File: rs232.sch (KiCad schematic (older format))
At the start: 7 parts, among them Q1 BC847, U4 MAX3188EEUT+T

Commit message: Use smaller jumper
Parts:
- removed JP2: SolderJumper_2_Bridged, Jumpers:SMT-JUMPER_2_NO_SILK, symbol Jumper:SolderJumper_2_Bridged
- JP1: footprint Connector_PinHeader_2.54mm:PinHeader_2x01_P2.54mm_Vertical -> Connector_PinHeader_1.00mm:PinHeader_1x02_P1.00mm_Vertical
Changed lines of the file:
@@
 $Descr A4 11693 8268
 encoding utf-8
-Sheet 5 5
+Sheet 4 5
 Title ""
 Date ""
@@
 F 0 "JP1" H 5600 3953 50  0000 C CNN
 F 1 "Jumper_2_Bridged" H 5600 3954 50  0001 C CNN
-F 2 "Connector_PinHeader_2.54mm:PinHeader_2x01_P2.54mm_Vertical" H 5600 3850 50  0001 C CNN
+F 2 "Connector_PinHeader_1.00mm:PinHeader_1x02_P1.00mm_Vertical" H 5600 3850 50  0001 C CNN
 F 3 "~" H 5600 3850 50  0001 C CNN
 	1    5600 3850
@@
 Wire Wire Line
 	5350 2900 6300 2900
-Wire Wire Line
-	5250 3850 5400 3850
 $Comp
 L Device:R R?
@@
 Wire Wire Line
 	5400 4750 5400 4900
-$Comp
-L Jumper:SolderJumper_2_Bridged JP?
-U 1 1 5ED0E3F3
-P 5600 4000
-AR Path="/5ED0E3F3" Ref="JP?"  Part="1"
-AR Path="/5ED01473/5ED0E3F3" Ref="JP2"  Part="1"
-F 0 "JP2" H 5600 4113 50  0000 C CNN
-F 1 "SolderJumper_2_Bridged" H 5600 4114 50  0001 C CNN
-F 2 "Jumpers:SMT-JUMPER_2_NO_SILK" H 5600 4000 50  0001 C CNN
-F 3 "~" H 5600 4000 50  0001 C CNN
-	1    5600 4000
-	1    0    0    -1
-$EndComp
 Wire Notes Line
 	6500 3700 6500 4100
 Wire Notes Line
 	5200 3700 5200 4100
-Wire Wire Line
-	5450 4000 5250 4000
-Wire Wire Line
-	5250 4000 5250 3850
-Wire Wire Line
-	5750 4000 5950 4000
-Wire Wire Line
-	5950 3850 5950 4000
-Wire Wire Line
-	5950 4000 5950 4200
-Connection ~ 5950 4000
 $Comp
 L Transistor_BJT:BC847 Q?
@@
 Text HLabel 5150 3850 0    50   BiDi ~ 0
 UPDI
-Wire Wire Line
-	5250 3850 5150 3850
-Connection ~ 5250 3850
 Text HLabel 5150 4900 0    50   Output ~ 0
 RX
@@
 	5400 4900 5150 4900
 Connection ~ 5400 4900
+Wire Wire Line
+	5950 3850 5950 4200
+Wire Wire Line
+	5150 3850 5400 3850
 $EndSCHEMATC

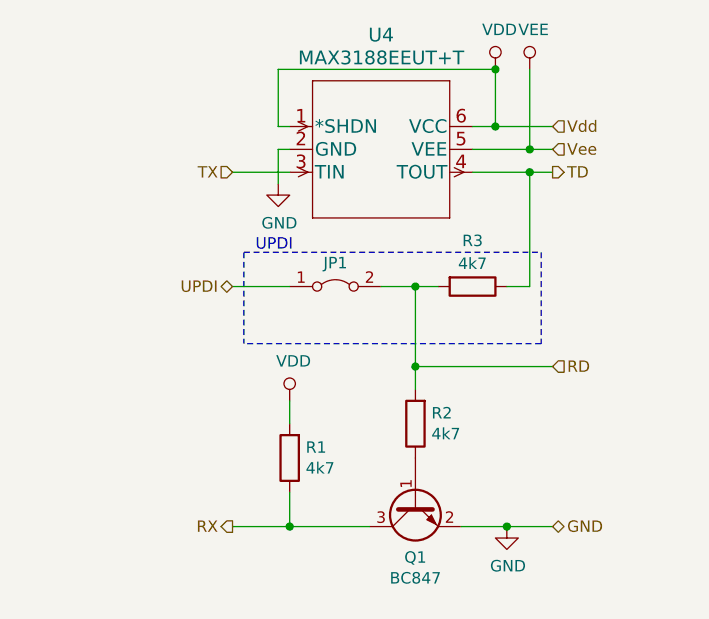
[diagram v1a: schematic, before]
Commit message: Use MAX3180 for incoming RS-232
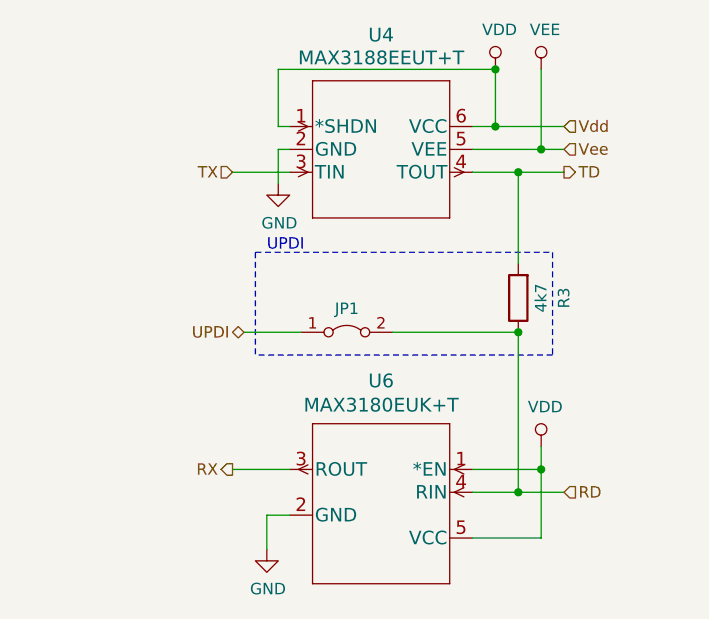
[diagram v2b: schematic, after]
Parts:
- removed Q1: BC847, Package_TO_SOT_SMD:SOT-23, symbol Transistor_BJT:BC847
- removed R1, R2: 4k7, Resistors_SMD:R_0603_HandSoldering, symbol Device:R
- added U6: MAX3180EUK+T, Package_TO_SOT_SMD:SOT-23-5_HandSoldering, symbol MAX3180:MAX3180EUK+T
- U4: footprint MAX3188:MAX3188EEUT&plus_T -> Package_TO_SOT_SMD:SOT-23-5_HandSoldering
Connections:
- net GND: now also U6.2 (GND)
- net RD: now also R3.1, U6.4 (RIN); no longer R3.2
- net RX: now also U6.3 (ROUT)
- net TD: now also R3.2; no longer R3.1
- net VDD: now also U6.1 (*EN), U6.5 (VCC)
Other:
- moved on the sheet: JP1, R3
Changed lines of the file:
@@
 L Jumper:Jumper_2_Bridged JP?
 U 1 1 5ED0E399
-P 5600 3850
+P 5650 4050
 AR Path="/5ED0E399" Ref="JP?"  Part="1"
 AR Path="/5ED01473/5ED0E399" Ref="JP1"  Part="1"
-F 0 "JP1" H 5600 3953 50  0000 C CNN
-F 1 "Jumper_2_Bridged" H 5600 3954 50  0001 C CNN
-F 2 "Connector_PinHeader_1.00mm:PinHeader_1x02_P1.00mm_Vertical" H 5600 3850 50  0001 C CNN
-F 3 "~" H 5600 3850 50  0001 C CNN
-	1    5600 3850
+F 0 "JP1" H 5650 4153 50  0000 C CNN
+F 1 "Jumper_2_Bridged" H 5650 4154 50  0001 C CNN
+F 2 "Connector_PinHeader_1.00mm:PinHeader_1x02_P1.00mm_Vertical" H 5650 4050 50  0001 C CNN
+F 3 "~" H 5650 4050 50  0001 C CNN
+	1    5650 4050
 	1    0    0    -1
 $EndComp
@@
 F 0 "U4" H 5800 3550 60  0000 C CNN
 F 1 "MAX3188EEUT+T" H 5800 3450 60  0000 C CNN
-F 2 "MAX3188:MAX3188EEUT&plus_T" H 6400 3390 60  0001 C CNN
+F 2 "Package_TO_SOT_SMD:SOT-23-5_HandSoldering" H 6400 3390 60  0001 C CNN
 F 3 "" H 5200 3150 60  0000 C CNN
 	1    5200 3150
@@
 $EndComp
 Wire Wire Line
-	6200 3250 6450 3250
+	6200 3250 6500 3250
 Wire Wire Line
-	6450 3250 6450 2900
+	6500 3250 6500 2900
 Wire Wire Line
 	6200 3150 6300 3150
@@
 Wire Wire Line
 	5150 3350 5400 3350
-Wire Wire Line
-	6200 3350 6450 3350
 Wire Wire Line
 	5400 3250 5350 3250
@@
 Wire Wire Line
 	5350 2900 6300 2900
-$Comp
-L Device:R R?
-U 1 1 5ED0E3C0
-P 5950 4450
-AR Path="/5ED0E3C0" Ref="R?"  Part="1"
-AR Path="/5ED01473/5ED0E3C0" Ref="R2"  Part="1"
-F 0 "R2" H 5880 4404 50  0000 R CNN
-F 1 "4k7" H 5880 4495 50  0000 R CNN
-F 2 "Resistors_SMD:R_0603_HandSoldering" V 5880 4450 50  0001 C CNN
-F 3 "~" H 5950 4450 50  0001 C CNN
-	1    5950 4450
-	-1   0    0    1
-$EndComp
-Wire Wire Line
-	5950 3850 5800 3850
-Wire Wire Line
-	6350 3850 6450 3850
-Wire Wire Line
-	6050 3850 5950 3850
-Connection ~ 5950 3850
 Wire Notes Line
-	5200 3700 6500 3700
+	5250 3700 6550 3700
 Wire Notes Line
-	6500 4100 5200 4100
-Text Notes 5250 3700 0    50   ~ 0
+	6550 4150 5250 4150
+Text Notes 5300 3700 0    50   ~ 0
 UPDI
-$Comp
-L Device:R R?
-U 1 1 5ED0E3D1
-P 6200 3850
-AR Path="/5ED0E3D1" Ref="R?"  Part="1"
-AR Path="/5ED01473/5ED0E3D1" Ref="R3"  Part="1"
-F 0 "R3" V 6000 3850 50  0000 C CNN
-F 1 "4k7" V 6100 3850 50  0000 C CNN
-F 2 "Resistors_SMD:R_0603_HandSoldering" V 6130 3850 50  0001 C CNN
-F 3 "~" H 6200 3850 50  0001 C CNN
-	1    6200 3850
-	0    1    1    0
-$EndComp
-$Comp
-L power:GND #PWR?
-U 1 1 5ED0E3D9
-P 6350 4900
-AR Path="/5ED0E3D9" Ref="#PWR?"  Part="1"
-AR Path="/5ED01473/5ED0E3D9" Ref="#PWR0105"  Part="1"
-F 0 "#PWR0105" H 6350 4650 50  0001 C CNN
-F 1 "GND" H 6355 4727 50  0000 C CNN
-F 2 "" H 6350 4900 50  0001 C CNN
-F 3 "" H 6350 4900 50  0001 C CNN
-	1    6350 4900
-	1    0    0    -1
-$EndComp
-$Comp
-L Device:R R?
-U 1 1 5ED0E3DF
-P 5400 4600
-AR Path="/5ED0E3DF" Ref="R?"  Part="1"
-AR Path="/5ED01473/5ED0E3DF" Ref="R1"  Part="1"
-F 0 "R1" H 5330 4554 50  0000 R CNN
-F 1 "4k7" H 5330 4645 50  0000 R CNN
-F 2 "Resistors_SMD:R_0603_HandSoldering" V 5330 4600 50  0001 C CNN
-F 3 "~" H 5400 4600 50  0001 C CNN
-	1    5400 4600
-	-1   0    0    1
-$EndComp
-$Comp
-L power:VDD #PWR?
-U 1 1 5ED0E3E5
-P 5400 4350
-AR Path="/5ED0E3E5" Ref="#PWR?"  Part="1"
-AR Path="/5ED01473/5ED0E3E5" Ref="#PWR0113"  Part="1"
-F 0 "#PWR0113" H 5400 4200 50  0001 C CNN
-F 1 "VDD" H 5417 4523 50  0000 C CNN
-F 2 "" H 5400 4350 50  0001 C CNN
-F 3 "" H 5400 4350 50  0001 C CNN
-	1    5400 4350
-	1    0    0    -1
-$EndComp
-Wire Wire Line
-	5400 4350 5400 4450
-Wire Wire Line
-	5950 4200 5950 4300
-Connection ~ 5950 4200
-Wire Wire Line
-	6150 4900 6350 4900
-Wire Wire Line
-	5400 4900 5750 4900
-Wire Wire Line
-	5400 4750 5400 4900
-Wire Notes Line
-	6500 3700 6500 4100
-Wire Notes Line
-	5200 3700 5200 4100
-$Comp
-L Transistor_BJT:BC847 Q?
-U 1 1 5ED0E402
-P 5950 4800
-AR Path="/5ED0E402" Ref="Q?"  Part="1"
-AR Path="/5ED01473/5ED0E402" Ref="Q1"  Part="1"
-F 0 "Q1" V 6185 4800 50  0000 C CNN
-F 1 "BC847" V 6276 4800 50  0000 C CNN
-F 2 "Package_TO_SOT_SMD:SOT-23" H 6150 4725 50  0001 L CIN
-F 3 "http://www.infineon.com/dgdl/Infineon-BC847SERIES_BC848SERIES_BC849SERIES_BC850SERIES-DS-v01_01-en.pdf?fileId=db3a304314dca389011541d4630a1657" H 5950 4800 50  0001 L CNN
-	1    5950 4800
-	0    -1   1    0
-$EndComp
-Text HLabel 6550 3350 2    50   Output ~ 0
+Text HLabel 6600 3350 2    50   Output ~ 0
 TD
-Wire Wire Line
-	6450 3350 6550 3350
-Connection ~ 6450 3350
-Wire Wire Line
-	6450 3350 6450 3850
 Connection ~ 6300 2900
 $Comp
@@
 L power:VEE #PWR?
 U 1 1 5ED0E3AB
-P 6450 2900
+P 6500 2900
 AR Path="/5ED0E3AB" Ref="#PWR?"  Part="1"
 AR Path="/5ED01473/5ED0E3AB" Ref="#PWR0115"  Part="1"
-F 0 "#PWR0115" H 6450 2750 50  0001 C CNN
-F 1 "VEE" H 6467 3073 50  0000 C CNN
-F 2 "" H 6450 2900 50  0001 C CNN
-F 3 "" H 6450 2900 50  0001 C CNN
-	1    6450 2900
+F 0 "#PWR0115" H 6500 2750 50  0001 C CNN
+F 1 "VEE" H 6517 3073 50  0000 C CNN
+F 2 "" H 6500 2900 50  0001 C CNN
+F 3 "" H 6500 2900 50  0001 C CNN
+	1    6500 2900
 	1    0    0    -1
 $EndComp
-Text HLabel 6550 4900 2    50   BiDi ~ 0
-GND
-Wire Wire Line
-	6550 4900 6350 4900
-Connection ~ 6350 4900
 Text HLabel 5150 3350 0    50   Input ~ 0
 TX
-Text HLabel 6550 3250 2    50   Input ~ 0
+Text HLabel 6600 3250 2    50   Input ~ 0
 Vee
-Text HLabel 6550 3150 2    50   Input ~ 0
+Text HLabel 6600 3150 2    50   Input ~ 0
 Vdd
 Wire Wire Line
-	6300 3150 6550 3150
+	6300 3150 6600 3150
 Connection ~ 6300 3150
 Wire Wire Line
-	6450 3250 6550 3250
-Connection ~ 6450 3250
-Text HLabel 6550 4200 2    50   Input ~ 0
+	6500 3250 6600 3250
+Connection ~ 6500 3250
+Text HLabel 6600 4750 2    50   Input ~ 0
 RD
-Wire Wire Line
-	5950 4200 6550 4200
-Text HLabel 5150 3850 0    50   BiDi ~ 0
+Text HLabel 5200 4050 0    50   BiDi ~ 0
 UPDI
-Text HLabel 5150 4900 0    50   Output ~ 0
+Text HLabel 5150 4650 0    50   Output ~ 0
 RX
 Wire Wire Line
-	5400 4900 5150 4900
-Connection ~ 5400 4900
+	5200 4050 5450 4050
+$Comp
+L MAX3180:MAX3180EUK+T U6
+U 1 1 5DF24D13
+P 6400 4650
+F 0 "U6" H 7000 5037 60  0000 C CNN
+F 1 "MAX3180EUK+T" H 7000 4931 60  0000 C CNN
+F 2 "Package_TO_SOT_SMD:SOT-23-5_HandSoldering" H 7200 4890 60  0001 C CNN
+F 3 "" H 6400 4650 60  0000 C CNN
+	1    6400 4650
+	-1   0    0    -1
+$EndComp
 Wire Wire Line
-	5950 3850 5950 4200
+	6500 4650 6500 4950
+$Comp
+L power:VDD #PWR?
+U 1 1 5DF2A05E
+P 6500 4550
+AR Path="/5DF2A05E" Ref="#PWR?"  Part="1"
+AR Path="/5ED01473/5DF2A05E" Ref="#PWR0105"  Part="1"
+F 0 "#PWR0105" H 6500 4400 50  0001 C CNN
+F 1 "VDD" H 6518 4723 50  0000 C CNN
+F 2 "" H 6500 4550 50  0001 C CNN
+F 3 "" H 6500 4550 50  0001 C CNN
+	1    6500 4550
+	1    0    0    -1
+$EndComp
 Wire Wire Line
-	5150 3850 5400 3850
+	6500 4650 6500 4550
+Connection ~ 6500 4650
+Wire Wire Line
+	6200 4650 6500 4650
+Wire Wire Line
+	6200 4950 6500 4950
+Wire Wire Line
+	5150 4650 5400 4650
+$Comp
+L Device:R R?
+U 1 1 5ED0E3D1
+P 6400 3900
+AR Path="/5ED0E3D1" Ref="R?"  Part="1"
+AR Path="/5ED01473/5ED0E3D1" Ref="R3"  Part="1"
+F 0 "R3" V 6200 3900 50  0000 C CNN
+F 1 "4k7" V 6300 3900 50  0000 C CNN
+F 2 "Resistors_SMD:R_0603_HandSoldering" V 6330 3900 50  0001 C CNN
+F 3 "~" H 6400 3900 50  0001 C CNN
+	1    6400 3900
+	-1   0    0    1
+$EndComp
+Wire Wire Line
+	6200 3350 6400 3350
+Wire Wire Line
+	6400 3750 6400 3350
+Connection ~ 6400 3350
+Wire Wire Line
+	6400 3350 6600 3350
+Wire Wire Line
+	5850 4050 6400 4050
+Wire Notes Line
+	6550 3700 6550 4150
+Wire Notes Line
+	5250 3700 5250 4150
+Wire Wire Line
+	6600 4750 6400 4750
+Connection ~ 6400 4050
+Wire Wire Line
+	6400 4050 6400 4750
+Connection ~ 6400 4750
+Wire Wire Line
+	6400 4750 6200 4750
+$Comp
+L power:GND #PWR?
+U 1 1 5DF382A6
+P 5300 5000
+AR Path="/5DF382A6" Ref="#PWR?"  Part="1"
+AR Path="/5ED01473/5DF382A6" Ref="#PWR0113"  Part="1"
+F 0 "#PWR0113" H 5300 4750 50  0001 C CNN
+F 1 "GND" H 5305 4827 50  0000 C CNN
+F 2 "" H 5300 5000 50  0001 C CNN
+F 3 "" H 5300 5000 50  0001 C CNN
+	1    5300 5000
+	1    0    0    -1
+$EndComp
+Wire Wire Line
+	5400 4850 5300 4850
+Wire Wire Line
+	5300 4850 5300 5000
 $EndSCHEMATC

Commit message: Completely routed with new chips
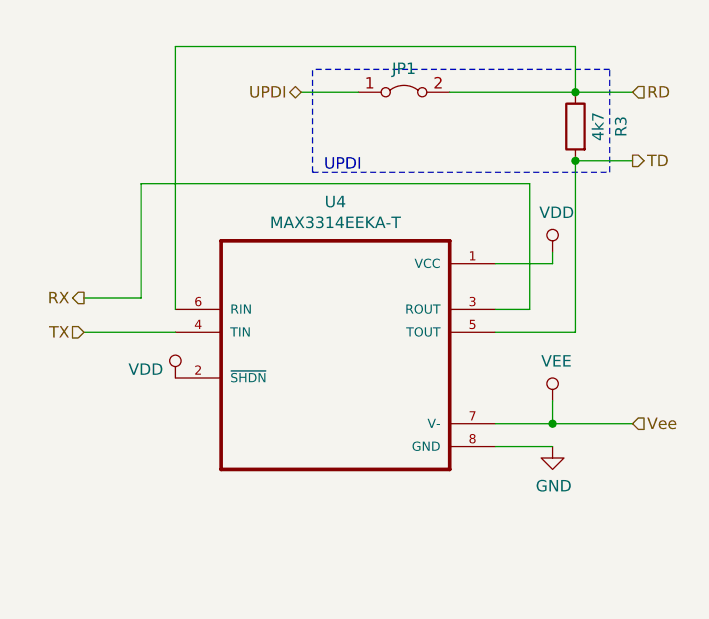
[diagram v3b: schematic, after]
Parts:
- removed U4: MAX3188EEUT+T, Package_TO_SOT_SMD:SOT-23-5_HandSoldering, symbol MAX3188:MAX3188EEUT+T
- removed U6: MAX3180EUK+T, Package_TO_SOT_SMD:SOT-23-5_HandSoldering, symbol MAX3180:MAX3180EUK+T
- added U4: MAX3314EEKA-T, SOT65P280X145-8N, symbol MAX3314EEKA-T:MAX3314EEKA-T
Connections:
- net GND: now also U4.8 (GND)
- net RD: now also U4.6 (RIN)
- net RX: now also U4.3 (ROUT)
- net TD: now also U4.5 (TOUT)
- net TX: now also U4.4 (TIN)
- net VDD: now also U4.1 (VCC), U4.2 (~SHDN~)
- net VEE: now also U4.7 (V-)
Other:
- moved on the sheet: JP1, R3
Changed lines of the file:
@@
 $EndDescr
-$Comp
-L power:GND #PWR?
-U 1 1 5ED0E38F
-P 5350 3400
-AR Path="/5ED0E38F" Ref="#PWR?"  Part="1"
-AR Path="/5ED01473/5ED0E38F" Ref="#PWR0104"  Part="1"
-F 0 "#PWR0104" H 5350 3150 50  0001 C CNN
-F 1 "GND" H 5355 3227 50  0000 C CNN
-F 2 "" H 5350 3400 50  0001 C CNN
-F 3 "" H 5350 3400 50  0001 C CNN
-	1    5350 3400
-	1    0    0    -1
-$EndComp
 $Comp
 L Jumper:Jumper_2_Bridged JP?
 U 1 1 5ED0E399
-P 5650 4050
+P 5900 3000
 AR Path="/5ED0E399" Ref="JP?"  Part="1"
 AR Path="/5ED01473/5ED0E399" Ref="JP1"  Part="1"
-F 0 "JP1" H 5650 4153 50  0000 C CNN
-F 1 "Jumper_2_Bridged" H 5650 4154 50  0001 C CNN
-F 2 "Connector_PinHeader_1.00mm:PinHeader_1x02_P1.00mm_Vertical" H 5650 4050 50  0001 C CNN
-F 3 "~" H 5650 4050 50  0001 C CNN
-	1    5650 4050
+F 0 "JP1" H 5900 3103 50  0000 C CNN
+F 1 "Jumper_2_Bridged" H 5900 3104 50  0001 C CNN
+F 2 "Connector_PinHeader_1.00mm:PinHeader_1x02_P1.00mm_Vertical" H 5900 3000 50  0001 C CNN
+F 3 "~" H 5900 3000 50  0001 C CNN
+	1    5900 3000
 	1    0    0    -1
 $EndComp
-$Comp
-L MAX3188:MAX3188EEUT+T U?
-U 1 1 5ED0E39F
-P 5200 3150
-AR Path="/5ED0E39F" Ref="U?"  Part="1"
-AR Path="/5ED01473/5ED0E39F" Ref="U4"  Part="1"
-F 0 "U4" H 5800 3550 60  0000 C CNN
-F 1 "MAX3188EEUT+T" H 5800 3450 60  0000 C CNN
-F 2 "Package_TO_SOT_SMD:SOT-23-5_HandSoldering" H 6400 3390 60  0001 C CNN
-F 3 "" H 5200 3150 60  0000 C CNN
-	1    5200 3150
-	1    0    0    -1
-$EndComp
-Wire Wire Line
-	6200 3250 6500 3250
-Wire Wire Line
-	6500 3250 6500 2900
-Wire Wire Line
-	6200 3150 6300 3150
-Wire Wire Line
-	6300 3150 6300 2900
-Wire Wire Line
-	5150 3350 5400 3350
-Wire Wire Line
-	5400 3250 5350 3250
-Wire Wire Line
-	5350 3250 5350 3400
-Wire Wire Line
-	5400 3150 5350 3150
-Wire Wire Line
-	5350 3150 5350 2900
-Wire Wire Line
-	5350 2900 6300 2900
 Wire Notes Line
-	5250 3700 6550 3700
+	5500 3350 6800 3350
 Wire Notes Line
-	6550 4150 5250 4150
-Text Notes 5300 3700 0    50   ~ 0
+	6800 2900 5500 2900
+Text Notes 5550 3350 0    50   ~ 0
 UPDI
-Text HLabel 6600 3350 2    50   Output ~ 0
+Text HLabel 6900 3300 2    50   Output ~ 0
 TD
-Connection ~ 6300 2900
 $Comp
 L power:VDD #PWR?
 U 1 1 5ED0E3A5
-P 6300 2900
+P 6550 3700
 AR Path="/5ED0E3A5" Ref="#PWR?"  Part="1"
 AR Path="/5ED01473/5ED0E3A5" Ref="#PWR0114"  Part="1"
-F 0 "#PWR0114" H 6300 2750 50  0001 C CNN
-F 1 "VDD" H 6318 3073 50  0000 C CNN
-F 2 "" H 6300 2900 50  0001 C CNN
-F 3 "" H 6300 2900 50  0001 C CNN
-	1    6300 2900
+F 0 "#PWR0114" H 6550 3550 50  0001 C CNN
+F 1 "VDD" H 6568 3873 50  0000 C CNN
+F 2 "" H 6550 3700 50  0001 C CNN
+F 3 "" H 6550 3700 50  0001 C CNN
+	1    6550 3700
 	1    0    0    -1
 $EndComp
@@
 L power:VEE #PWR?
 U 1 1 5ED0E3AB
-P 6500 2900
+P 6550 4350
 AR Path="/5ED0E3AB" Ref="#PWR?"  Part="1"
 AR Path="/5ED01473/5ED0E3AB" Ref="#PWR0115"  Part="1"
-F 0 "#PWR0115" H 6500 2750 50  0001 C CNN
-F 1 "VEE" H 6517 3073 50  0000 C CNN
-F 2 "" H 6500 2900 50  0001 C CNN
-F 3 "" H 6500 2900 50  0001 C CNN
-	1    6500 2900
+F 0 "#PWR0115" H 6550 4200 50  0001 C CNN
+F 1 "VEE" H 6567 4523 50  0000 C CNN
+F 2 "" H 6550 4350 50  0001 C CNN
+F 3 "" H 6550 4350 50  0001 C CNN
+	1    6550 4350
 	1    0    0    -1
 $EndComp
-Text HLabel 5150 3350 0    50   Input ~ 0
+Text HLabel 4500 4050 0    50   Input ~ 0
 TX
-Text HLabel 6600 3250 2    50   Input ~ 0
+Text HLabel 6900 4450 2    50   Input ~ 0
 Vee
-Text HLabel 6600 3150 2    50   Input ~ 0
-Vdd
-Wire Wire Line
-	6300 3150 6600 3150
-Connection ~ 6300 3150
-Wire Wire Line
-	6500 3250 6600 3250
-Connection ~ 6500 3250
-Text HLabel 6600 4750 2    50   Input ~ 0
+Text HLabel 6900 3000 2    50   Input ~ 0
 RD
-Text HLabel 5200 4050 0    50   BiDi ~ 0
+Text HLabel 5450 3000 0    50   BiDi ~ 0
 UPDI
-Text HLabel 5150 4650 0    50   Output ~ 0
+Text HLabel 4500 3900 0    50   Output ~ 0
 RX
 Wire Wire Line
-	5200 4050 5450 4050
+	5450 3000 5700 3000
+Wire Wire Line
+	6100 3000 6650 3000
+Wire Notes Line
+	6800 3350 6800 2900
+Wire Notes Line
+	5500 3350 5500 2900
+Connection ~ 6650 3000
 $Comp
-L MAX3180:MAX3180EUK+T U6
-U 1 1 5DF24D13
-P 6400 4650
-F 0 "U6" H 7000 5037 60  0000 C CNN
-F 1 "MAX3180EUK+T" H 7000 4931 60  0000 C CNN
-F 2 "Package_TO_SOT_SMD:SOT-23-5_HandSoldering" H 7200 4890 60  0001 C CNN
-F 3 "" H 6400 4650 60  0000 C CNN
-	1    6400 4650
+L power:GND #PWR?
+U 1 1 5DF382A6
+P 6550 4550
+AR Path="/5DF382A6" Ref="#PWR?"  Part="1"
+AR Path="/5ED01473/5DF382A6" Ref="#PWR0113"  Part="1"
+F 0 "#PWR0113" H 6550 4300 50  0001 C CNN
+F 1 "GND" H 6555 4377 50  0000 C CNN
+F 2 "" H 6550 4550 50  0001 C CNN
+F 3 "" H 6550 4550 50  0001 C CNN
+	1    6550 4550
+	1    0    0    -1
+$EndComp
+$Comp
+L MAX3314EEKA-T:MAX3314EEKA-T U4
+U 1 1 5DF544D0
+P 5600 4150
+F 0 "U4" H 5600 4820 50  0000 C CNN
+F 1 "MAX3314EEKA-T" H 5600 4729 50  0000 C CNN
+F 2 "SOT65P280X145-8N" H 5600 4150 50  0001 L BNN
+F 3 "Maxim Integrated" H 5600 4150 50  0001 L BNN
+F 4 "SOT-23-8 Maxim" H 5600 4150 50  0001 L BNN "Field4"
+F 5 "MAX3314EEKA+TCT-ND" H 5600 4150 50  0001 L BNN "Field5"
+F 6 "Single Transmitter/Receiver RS-232 8-Pin SOT-23 T/R" H 5600 4150 50  0001 L BNN "Field6"
+F 7 "https://www.digikey.com/product-detail/en/maxim-integrated/MAX3314EEKA-T/MAX3314EEKA-TCT-ND/5820996?utm_source=snapeda&utm_medium=aggregator&utm_campaign=symbol" H 5600 4150 50  0001 L BNN "Field7"
+F 8 "MAX3314EEKA+T" H 5600 4150 50  0001 L BNN "Field8"
+	1    5600 4150
+	1    0    0    -1
+$EndComp
+Wire Wire Line
+	6650 3000 6900 3000
+Wire Wire Line
+	6650 3300 6900 3300
+$Comp
+L Device:R R?
+U 1 1 5ED0E3D1
+P 6650 3150
+AR Path="/5ED0E3D1" Ref="R?"  Part="1"
+AR Path="/5ED01473/5ED0E3D1" Ref="R3"  Part="1"
+F 0 "R3" V 6450 3150 50  0000 C CNN
+F 1 "4k7" V 6550 3150 50  0000 C CNN
+F 2 "Resistors_SMD:R_0603_HandSoldering" V 6580 3150 50  0001 C CNN
+F 3 "~" H 6650 3150 50  0001 C CNN
+	1    6650 3150
 	-1   0    0    -1
 $EndComp
 Wire Wire Line
-	6500 4650 6500 4950
+	6650 3300 6650 4050
+Wire Wire Line
+	6650 4050 6300 4050
+Connection ~ 6650 3300
+Wire Wire Line
+	6650 3000 6650 2800
+Wire Wire Line
+	6650 2800 4900 2800
+Wire Wire Line
+	4900 2800 4900 3950
+Wire Wire Line
+	6300 3950 6450 3950
+Wire Wire Line
+	6450 3950 6450 3400
+Wire Wire Line
+	6450 3400 4750 3400
+Wire Wire Line
+	4750 3400 4750 3900
+Wire Wire Line
+	4750 3900 4500 3900
+Wire Wire Line
+	4500 4050 4900 4050
+Wire Wire Line
+	6900 4450 6550 4450
+Wire Wire Line
+	6550 4350 6550 4450
+Connection ~ 6550 4450
+Wire Wire Line
+	6550 4450 6300 4450
+Wire Wire Line
+	6550 4550 6300 4550
+Wire Wire Line
+	6300 3750 6550 3750
+Wire Wire Line
+	6550 3750 6550 3700
 $Comp
 L power:VDD #PWR?
-U 1 1 5DF2A05E
-P 6500 4550
-AR Path="/5DF2A05E" Ref="#PWR?"  Part="1"
-AR Path="/5ED01473/5DF2A05E" Ref="#PWR0105"  Part="1"
-F 0 "#PWR0105" H 6500 4400 50  0001 C CNN
-F 1 "VDD" H 6518 4723 50  0000 C CNN
-F 2 "" H 6500 4550 50  0001 C CNN
-F 3 "" H 6500 4550 50  0001 C CNN
-	1    6500 4550
+U 1 1 5DF679F4
+P 4900 4250
+AR Path="/5DF679F4" Ref="#PWR?"  Part="1"
+AR Path="/5ED01473/5DF679F4" Ref="#PWR0104"  Part="1"
+F 0 "#PWR0104" H 4900 4100 50  0001 C CNN
+F 1 "VDD" H 4847 4287 50  0000 R CNN
+F 2 "" H 4900 4250 50  0001 C CNN
+F 3 "" H 4900 4250 50  0001 C CNN
+	1    4900 4250
 	1    0    0    -1
 $EndComp
-Wire Wire Line
-	6500 4650 6500 4550
-Connection ~ 6500 4650
-Wire Wire Line
-	6200 4650 6500 4650
-Wire Wire Line
-	6200 4950 6500 4950
-Wire Wire Line
-	5150 4650 5400 4650
-$Comp
-L Device:R R?
-U 1 1 5ED0E3D1
-P 6400 3900
-AR Path="/5ED0E3D1" Ref="R?"  Part="1"
-AR Path="/5ED01473/5ED0E3D1" Ref="R3"  Part="1"
-F 0 "R3" V 6200 3900 50  0000 C CNN
-F 1 "4k7" V 6300 3900 50  0000 C CNN
-F 2 "Resistors_SMD:R_0603_HandSoldering" V 6330 3900 50  0001 C CNN
-F 3 "~" H 6400 3900 50  0001 C CNN
-	1    6400 3900
-	-1   0    0    1
-$EndComp
-Wire Wire Line
-	6200 3350 6400 3350
-Wire Wire Line
-	6400 3750 6400 3350
-Connection ~ 6400 3350
-Wire Wire Line
-	6400 3350 6600 3350
-Wire Wire Line
-	5850 4050 6400 4050
-Wire Notes Line
-	6550 3700 6550 4150
-Wire Notes Line
-	5250 3700 5250 4150
-Wire Wire Line
-	6600 4750 6400 4750
-Connection ~ 6400 4050
-Wire Wire Line
-	6400 4050 6400 4750
-Connection ~ 6400 4750
-Wire Wire Line
-	6400 4750 6200 4750
-$Comp
-L power:GND #PWR?
-U 1 1 5DF382A6
-P 5300 5000
-AR Path="/5DF382A6" Ref="#PWR?"  Part="1"
-AR Path="/5ED01473/5DF382A6" Ref="#PWR0113"  Part="1"
-F 0 "#PWR0113" H 5300 4750 50  0001 C CNN
-F 1 "GND" H 5305 4827 50  0000 C CNN
-F 2 "" H 5300 5000 50  0001 C CNN
-F 3 "" H 5300 5000 50  0001 C CNN
-	1    5300 5000
-	1    0    0    -1
-$EndComp
-Wire Wire Line
-	5400 4850 5300 4850
-Wire Wire Line
-	5300 4850 5300 5000
 $EndSCHEMATC
